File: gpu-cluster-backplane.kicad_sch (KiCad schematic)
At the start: 69 parts, among them J1 4PIN-22-27-2041, J10 10107844-002LF, J11 4PIN-22-27-2041, J12 4PIN-22-27-2041, J13 4PIN-22-27-2041, J14 4PIN-22-27-2041, J2 BM04B-SRSS-TB-LF-SN, J3 BM04B-SRSS-TB-LF-SN, J4 39288080, J5 39288080, J6 39288080, J7 39288080, J8 39288080, Q11 BC856,215

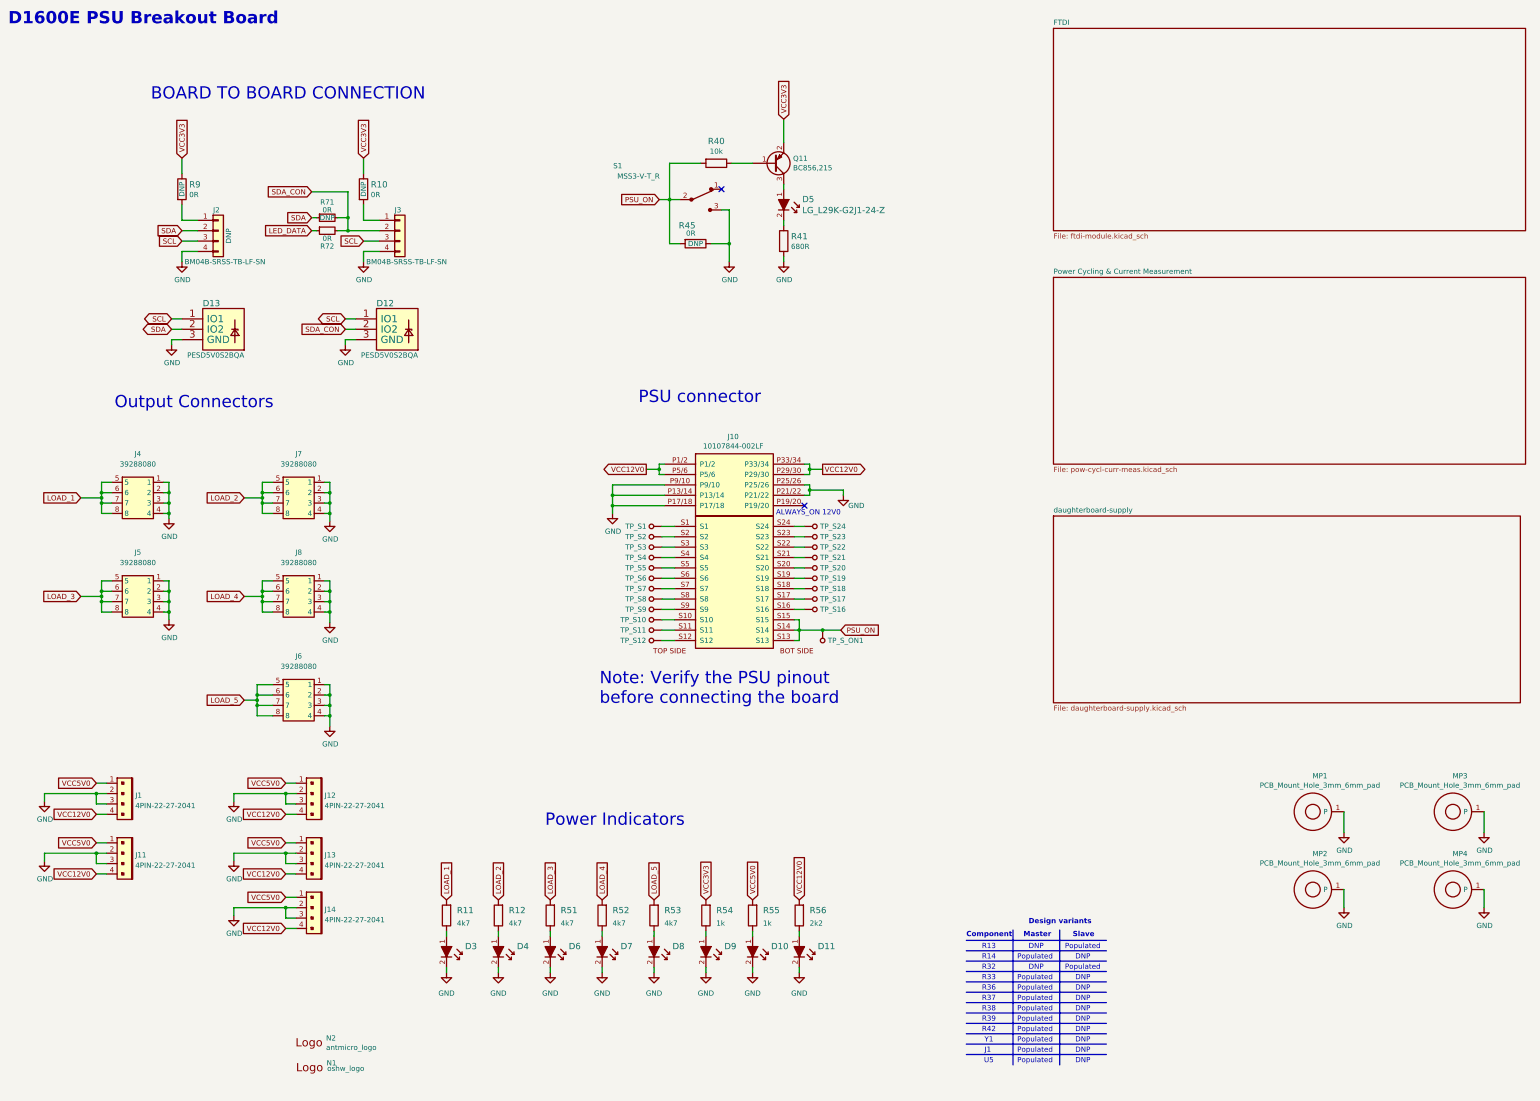
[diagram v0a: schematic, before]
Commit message: Perform globlib and find alterante components
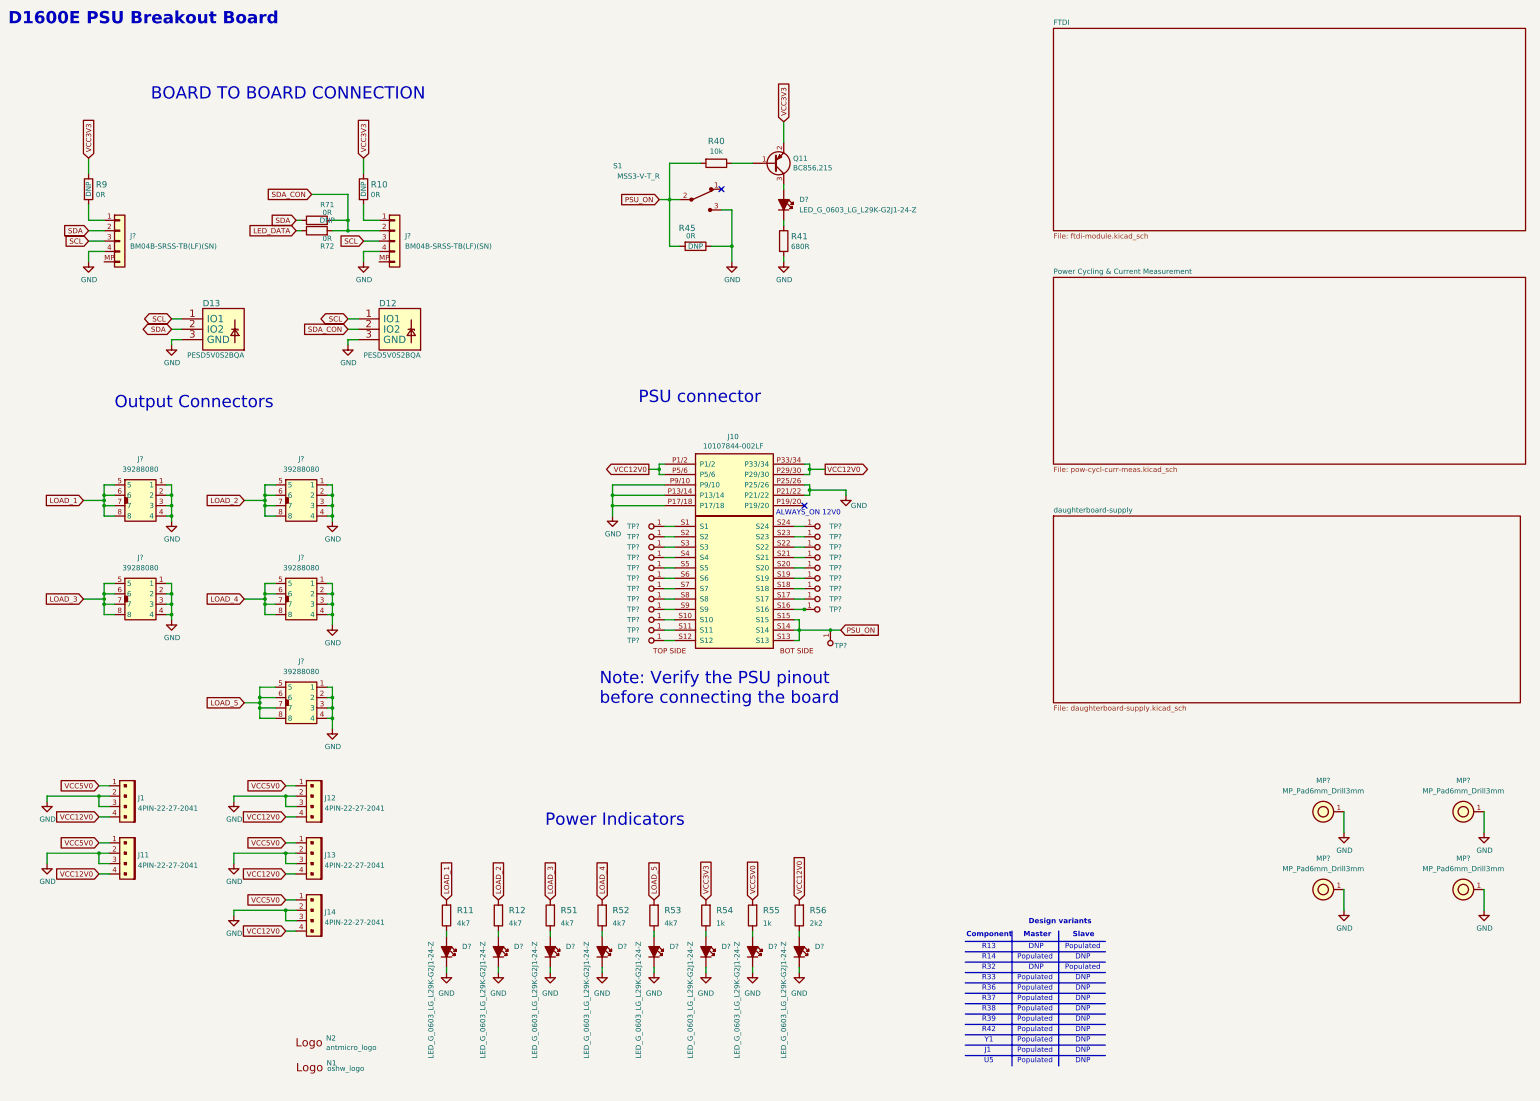
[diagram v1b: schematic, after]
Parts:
- removed D10, D11, D3, D4, D5, D6, D7, D8, D9: LG_L29K-G2J1-24-Z, gpu-cluster-backplane-footprints:LED_0603, symbol gpu-cluster-backplane:LG_L29K-G2J1-24-Z
- removed J2, J3: BM04B-SRSS-TB-LF-SN, gpu-cluster-backplane-footprints:BM04B-SRSS-TB-LF-SN, symbol gpu-cluster-backplane:BM04B-SRSS-TB-LF-SN
- removed J4, J5, J6, J7, J8: 39288080, gpu-cluster-backplane-footprints:MOLEX_39288080, symbol gpu-cluster-backplane:39288080
- removed MP1, MP2, MP3, MP4: PCB_Mount_Hole_3mm_6mm_pad, gpu-cluster-backplane-footprints:mounting-hole-3.2mm, symbol gpu-cluster-backplane:PCB_Mount_Hole_3mm_6mm_pad
- removed TP_S1, TP_S10, TP_S11, TP_S12, TP_S16, TP_S17, TP_S18, TP_S19, TP_S2, TP_S20, TP_S21, TP_S22, TP_S23, TP_S24, TP_S3, TP_S4, TP_S5, TP_S6, TP_S7, TP_S8, TP_S9, TP_S_ON1: TP_SMD1MM, gpu-cluster-backplane-footprints:Testpoint_smd_1mm, symbol gpu-cluster-backplane:TP_SMD1MM
- added D? (x9): LED_G_0603_LG_L29K-G2J1-24-Z, antmicro-footprints:LED_0603_1608Metric_G, symbol antmicroLEDIndicationDiscrete:LED_G_0603_LG_L29K-G2J1-24-Z
- added J? (x5): 39288080, gpu-cluster-backplane-footprints:MOLEX_39288080, symbol gpu-cluster-backplane:39288080
- added J? (x2): JST_SH_1x4_BM04B-SRSS-TB-LF-SN, antmicro-footprints:Conn_JST_SH_1x4_BM04B-SRSS-TB-LF-SN, symbol antmicroWire2BoardConnectors:JST_SH_1x4_BM04B-SRSS-TB-LF-SN
- added MP? (x4): MP_Pad6mm_Drill3mm, antmicro-footprints:MP_Pad6mm_Drill3mm, symbol antmicroMechanicalParts:MP_Pad6mm_Drill3mm
- added TP? (x22): TP_1mm_SMD, antmicro-footprints:TP_SMD_1mm, symbol antmicroTestPoints:TP_1mm_SMD
- D12, D13: footprint gpu-cluster-backplane-footprints:TPD2E009DRTR -> antmicro-footprints:TPD2E009DRTR; symbol gpu-cluster-backplane:PESD5V0S2BQA -> antmicroTVSDiodes:PESD5V0S2BQA
- N1: footprint gpu-cluster-backplane-footprints:OSHW-Logo_7.5x8mm_Mask -> antmicro-footprints:oshw-logo; symbol gpu-cluster-backplane:oshw_logo -> antmicroMechanicalParts:oshw_logo
- N2: footprint gpu-cluster-backplane-footprints:antmicro-logo_scaled_20mm_mask -> antmicro-footprints:antmicro-logo; symbol gpu-cluster-backplane:antmicro_logo -> antmicroMechanicalParts:antmicro_logo
- R10, R45, R9: footprint gpu-cluster-backplane-footprints:0402-res -> antmicro-footprints:R_0402_1005Metric; symbol gpu-cluster-backplane:R_0R_0402 -> antmicroResistors0402:R_0R_0402
- R11, R12, R51, R52, R53: footprint gpu-cluster-backplane-footprints:0603-res -> antmicro-footprints:R_0603_1608Metric; symbol gpu-cluster-backplane:R_4k7_0603 -> antmicroResistors0603:R_4k7_0603
- R40: footprint gpu-cluster-backplane-footprints:0402-res -> antmicro-footprints:R_0402_1005Metric; symbol gpu-cluster-backplane:R_10k_0402 -> antmicroResistors0402:R_10k_0402
- R41: footprint gpu-cluster-backplane-footprints:0402-res -> antmicro-footprints:R_0402_1005Metric; symbol gpu-cluster-backplane:R_680R_0402 -> antmicroResistors0402:R_680R_0402
- R54, R55: footprint gpu-cluster-backplane-footprints:0603-res -> antmicro-footprints:R_0603_1608Metric; symbol gpu-cluster-backplane:R_1k_0603 -> antmicroResistors0603:R_1k_0603
- R56: footprint gpu-cluster-backplane-footprints:0603-res -> antmicro-footprints:R_0603_1608Metric; symbol gpu-cluster-backplane:R_2k2_0603 -> antmicroResistors0603:R_2k2_0603
- S1: footprint gpu-cluster-backplane-footprints:Switch_Slide_MSS3 -> antmicro-footprints:Switch_Slide_MSS3; symbol gpu-cluster-backplane:MSS3-V-T_R -> antmicroSlideSwitches:MSS3-V-T_R
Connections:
- net GND: now also D?.2, D?.2, D?.2, D?.2, D?.2, D?.2, D?.2, D?.2, J?.1, J?.1, J?.1, J?.1, J?.1, J?.2, J?.2, J?.2, J?.2, J?.2, J?.3, J?.3, J?.3, J?.3, J?.3, J?.4, J?.4, J?.4, J?.4, J?.4, J?.4 (Pin_4), J?.4 (Pin_4), MP?.1, MP?.1, MP?.1, MP?.1
- net LOAD_1: now also J?.5, J?.6, J?.7, J?.8
- net LOAD_2: now also J?.5, J?.6, J?.7, J?.8
- net LOAD_3: now also J?.5, J?.6, J?.7, J?.8
- net LOAD_4: now also J?.5, J?.6, J?.7, J?.8
- net LOAD_5: now also J?.5, J?.6, J?.7, J?.8
- net PSU_ON: now also TP?.1
- net SCL: now also J?.3 (Pin_3), J?.3 (Pin_3)
- net SDA: now also J?.2 (Pin_2)
- net SDA_CON: now also J?.2 (Pin_2)
- net at R9.2: now also J?.1 (Pin_1)
- net at R10.2: now also J?.1 (Pin_1)
- net at J10.S1: now also TP?.1
- net at J10.S10: now also TP?.1
- net at J10.S11: now also TP?.1
- net at J10.S12: now also TP?.1
- net at J10.S16: now also TP?.1
- net at J10.S17: now also TP?.1
- net at J10.S18: now also TP?.1
- net at J10.S19: now also TP?.1
- net at J10.S2: now also TP?.1
- net at J10.S20: now also TP?.1
- net at J10.S21: now also TP?.1
- net at J10.S22: now also TP?.1
- net at J10.S23: now also TP?.1
- net at J10.S24: now also TP?.1
- net at J10.S3: now also TP?.1
- net at J10.S4: now also TP?.1
- net at J10.S5: now also TP?.1
- net at J10.S6: now also TP?.1
- net at J10.S7: now also TP?.1
- net at J10.S8: now also TP?.1
- net at J10.S9: now also TP?.1
- net at Q11.3: now also D?.1
- net at R41.1: now also D?.2
- net at R53.1: now also D?.1
- net at R51.1: now also D?.1
- net at R11.1: now also D?.1
- net at R12.1: now also D?.1
- net at R52.1: now also D?.1
- net at R55.1: now also D?.1
- net at R56.1: now also D?.1
- net at R54.1: now also D?.1
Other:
- moved on the sheet: D12, J1, J11, J12, J14, R45, R71, R72, R9

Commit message: Removing unecessary parts of the schematic
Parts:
- removed D12: PESD5V0S2BQA, antmicro-footprints:TPD2E009DRTR, symbol antmicroTVSDiodes:PESD5V0S2BQA
- removed D? (x2): LED_G_0603_LG_L29K-G2J1-24-Z, antmicro-footprints:LED_0603_1608Metric_G, symbol antmicroLEDIndicationDiscrete:LED_G_0603_LG_L29K-G2J1-24-Z
- removed J1, J11, J12, J13, J14: 4PIN-22-27-2041, antmicro-footprints:4PIN-22-27-2041, symbol antmicroRectangularConnectorsHeadersMalePins:4PIN-22-27-2041
- removed J? (x2): JST_SH_1x4_BM04B-SRSS-TB-LF-SN, antmicro-footprints:Conn_JST_SH_1x4_BM04B-SRSS-TB-LF-SN, symbol antmicroWire2BoardConnectors:JST_SH_1x4_BM04B-SRSS-TB-LF-SN
- removed R10, R71, R72, R9: R_0R_0402, antmicro-footprints:R_0402_1005Metric, symbol antmicroResistors0402:R_0R_0402
- removed R54, R55: R_1k_0603, antmicro-footprints:R_0603_1608Metric, symbol antmicroResistors0603:R_1k_0603
- added D? (x3): LED_G_0603_LG_L29K-G2J1-24-Z, antmicro-footprints:LED_0603_1608Metric_G, symbol antmicroLEDIndicationDiscrete:LED_G_0603_LG_L29K-G2J1-24-Z
- added MP? (x12): MP_Pad6mm_Drill3mm, antmicro-footprints:MP_Pad6mm_Drill3mm, symbol antmicroMechanicalParts:MP_Pad6mm_Drill3mm
- added R? (x3): R_4k7_0603, antmicro-footprints:R_0603_1608Metric, symbol antmicroResistors0603:R_4k7_0603
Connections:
- net GND: now also D?.2, D?.2, D?.2, MP?.1, MP?.1, MP?.1, MP?.1, MP?.1, MP?.1, MP?.1, MP?.1, MP?.1, MP?.1, MP?.1, MP?.1
- new net: D?.1, R?.1 (x3)
- new net LOAD_6: R?.2
- new net LOAD_7: R?.2
- new net LOAD_8: R?.2
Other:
- removed sheet daughterboard-supply
- note added: "GPU Cluster Backplane"
- note removed: "BOARD TO BOARD CONNECTION"
- note removed: "Component"
- note removed: "D1600E PSU Breakout Board"
- note removed: "DNP"
- note removed: "Design variants"
- note removed: "J1"
- note removed: "Master"
- note removed: "Populated"
- note removed: "R13"
- note removed: "R14"
- note removed: "R32"
- note removed: "R33"
- note removed: "R36"
- note removed: "R37"
- note removed: "R38"
- note removed: "R39"
- note removed: "R42"
- note removed: "Slave"
- note removed: "U5"
- note removed: "Y1"
- title: D1600E PSU Breakout Board -> GPU Cluster Backplane
- moved on the sheet: D13, D?, J?, MP?, R56

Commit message: Updated schematic structure
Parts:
- removed D13: PESD5V0S2BQA, antmicro-footprints:TPD2E009DRTR, symbol antmicroTVSDiodes:PESD5V0S2BQA
- removed D? (x10): LED_G_0603_LG_L29K-G2J1-24-Z, antmicro-footprints:LED_0603_1608Metric_G, symbol antmicroLEDIndicationDiscrete:LED_G_0603_LG_L29K-G2J1-24-Z
- removed J10: 10107844-002LF, gpu-cluster-backplane-footprints:10107844-002LF, symbol gpu-cluster-backplane:10107844-002LF
- removed J? (x5): 39288080, gpu-cluster-backplane-footprints:MOLEX_39288080, symbol gpu-cluster-backplane:39288080
- removed MP? (x16): MP_Pad6mm_Drill3mm, antmicro-footprints:MP_Pad6mm_Drill3mm, symbol antmicroMechanicalParts:MP_Pad6mm_Drill3mm
- removed Q11: BC856,215, gpu-cluster-backplane-footprints:SOT-23-3, symbol gpu-cluster-backplane:BC856,215
- removed R11, R12, R51, R52, R53, R? (x3): R_4k7_0603, antmicro-footprints:R_0603_1608Metric, symbol antmicroResistors0603:R_4k7_0603
- removed R40: R_10k_0402, antmicro-footprints:R_0402_1005Metric, symbol antmicroResistors0402:R_10k_0402
- removed R41: R_680R_0402, antmicro-footprints:R_0402_1005Metric, symbol antmicroResistors0402:R_680R_0402
- removed R45: R_0R_0402, antmicro-footprints:R_0402_1005Metric, symbol antmicroResistors0402:R_0R_0402
- removed R56: R_2k2_0603, antmicro-footprints:R_0603_1608Metric, symbol antmicroResistors0603:R_2k2_0603
- removed S1: MSS3-V-T_R, antmicro-footprints:Switch_Slide_MSS3, symbol antmicroSlideSwitches:MSS3-V-T_R
- removed TP? (x22): TP_1mm_SMD, antmicro-footprints:TP_SMD_1mm, symbol antmicroTestPoints:TP_1mm_SMD
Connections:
- no-connect marks 2 -> 0
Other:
- added sheet connectors (connectors.kicad_sch)
- added sheet fans-control (fans-control.kicad_sch)
- added sheet mechanical (mechanical.kicad_sch)
- added sheet power-cycling (power-cycling.kicad_sch)
- added sheet voltage-and-current-measurement (voltage-and-current-measurement.kicad_sch)
- note removed: "ALWAYS_ON 12V0"
- note removed: "Note: Verify the PSU pinout before connecting the board"
- note removed: "Output Connectors"
- note removed: "PSU connector"
- note removed: "Power Indicators"

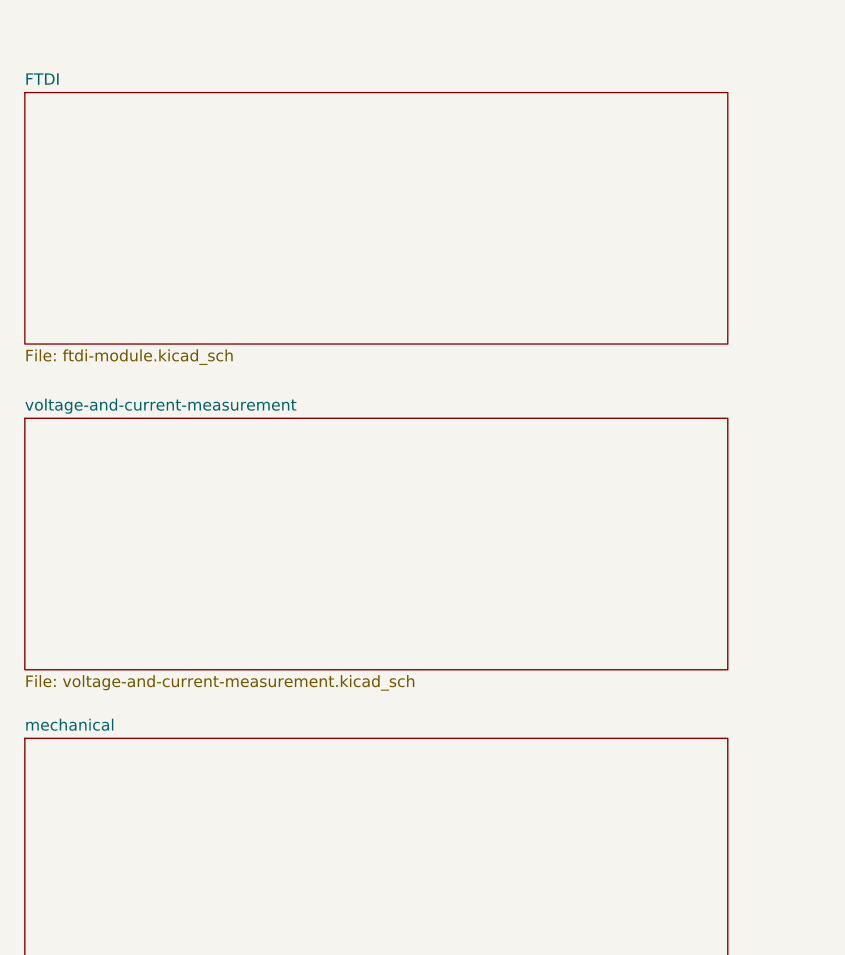
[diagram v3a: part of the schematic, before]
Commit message: Sch Voltage and current measurement
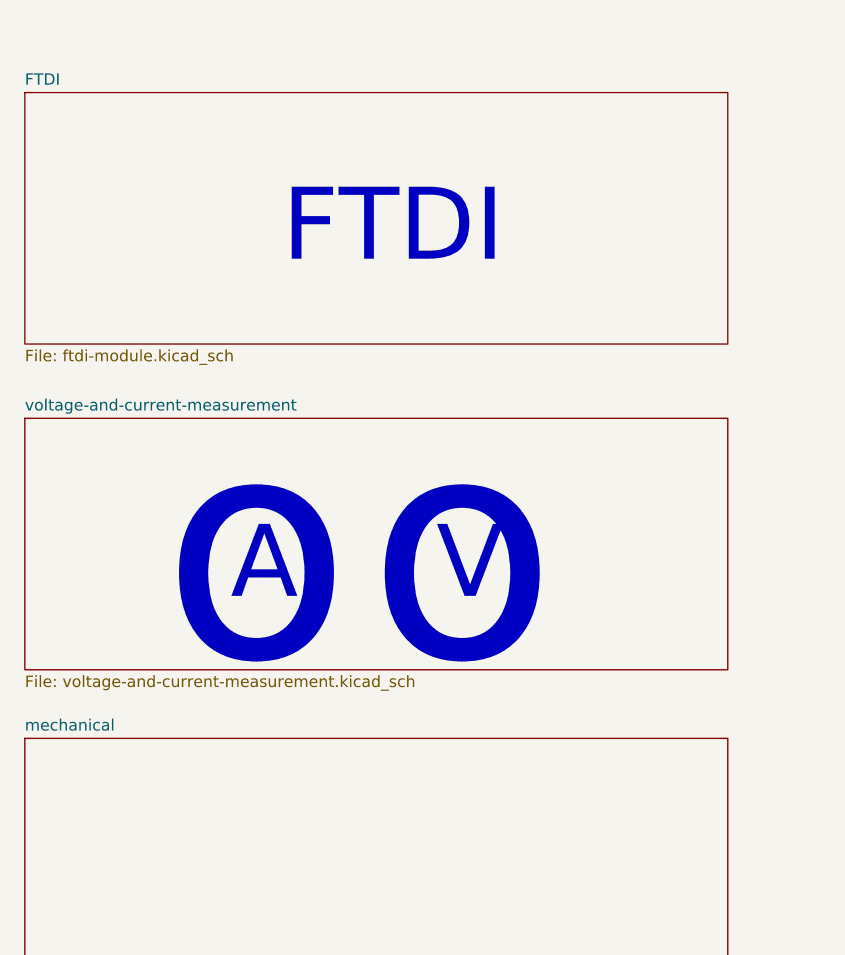
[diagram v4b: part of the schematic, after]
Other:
- note added: "A"
- note added: "FTDI"
- note added: "V"
- note added: "o"
